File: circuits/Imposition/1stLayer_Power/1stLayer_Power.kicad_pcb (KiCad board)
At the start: 2 copper layers, 62.9 x 90.7 mm, 53 parts, among them J1 Conn_01x14_Pin, J11 Conn_01x02_Male, J12 Conn_01x02_Male, J2 Conn_01x14_Pin, J3 Conn_01x10_Socket, J4 Conn_01x02_Male, J5 Conn_01x02_Male, J6 Conn_01x02_Male, J7 Conn_01x14_Pin, J8 Conn_01x08_MountingPin, J9 Conn_01x08_MountingPin, Q1 2N7002, Q4 SQS141ELNW, Q6 SQS141ELNW, SW1 SW_SPDT

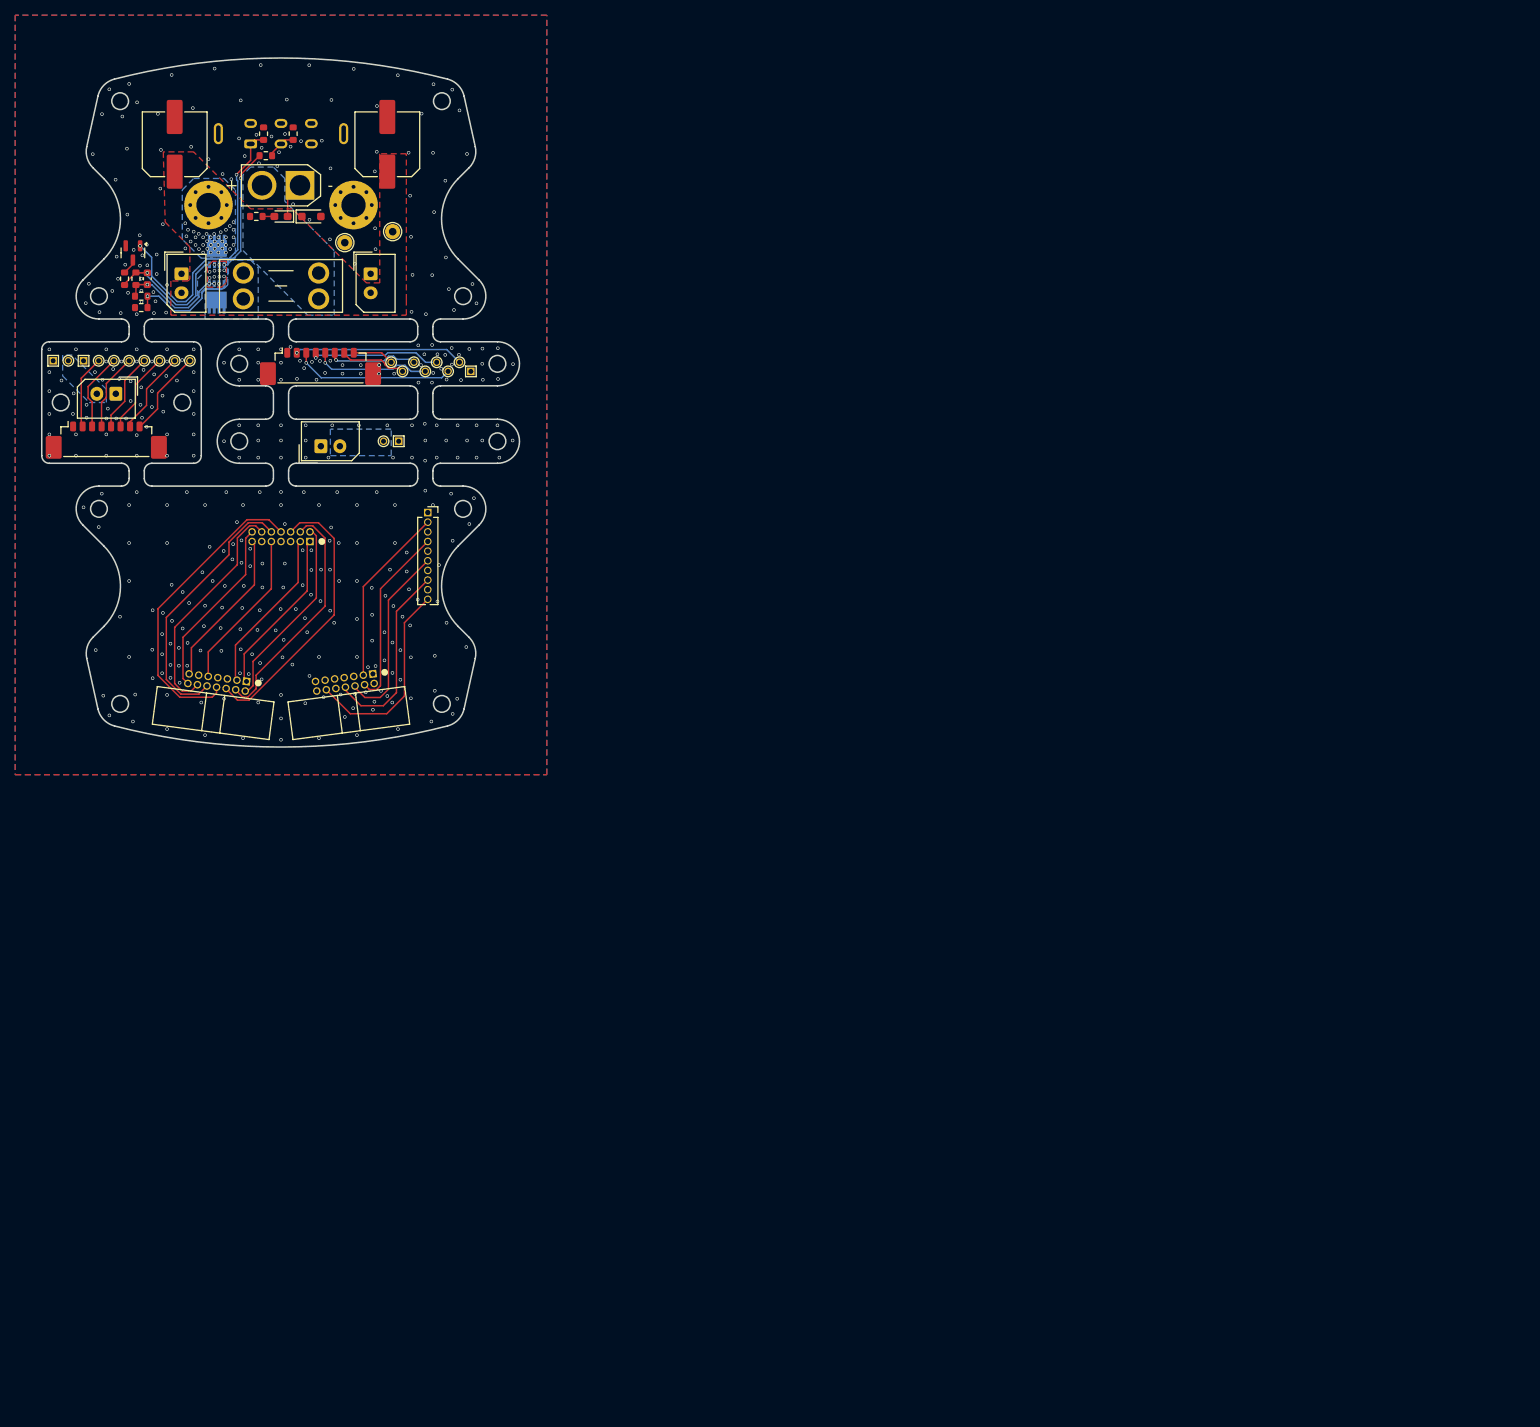
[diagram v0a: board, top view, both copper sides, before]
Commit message: 発注_第一弾
Drive, 1stLayer_Power, 2ndLayer_3rdLayer
を発注
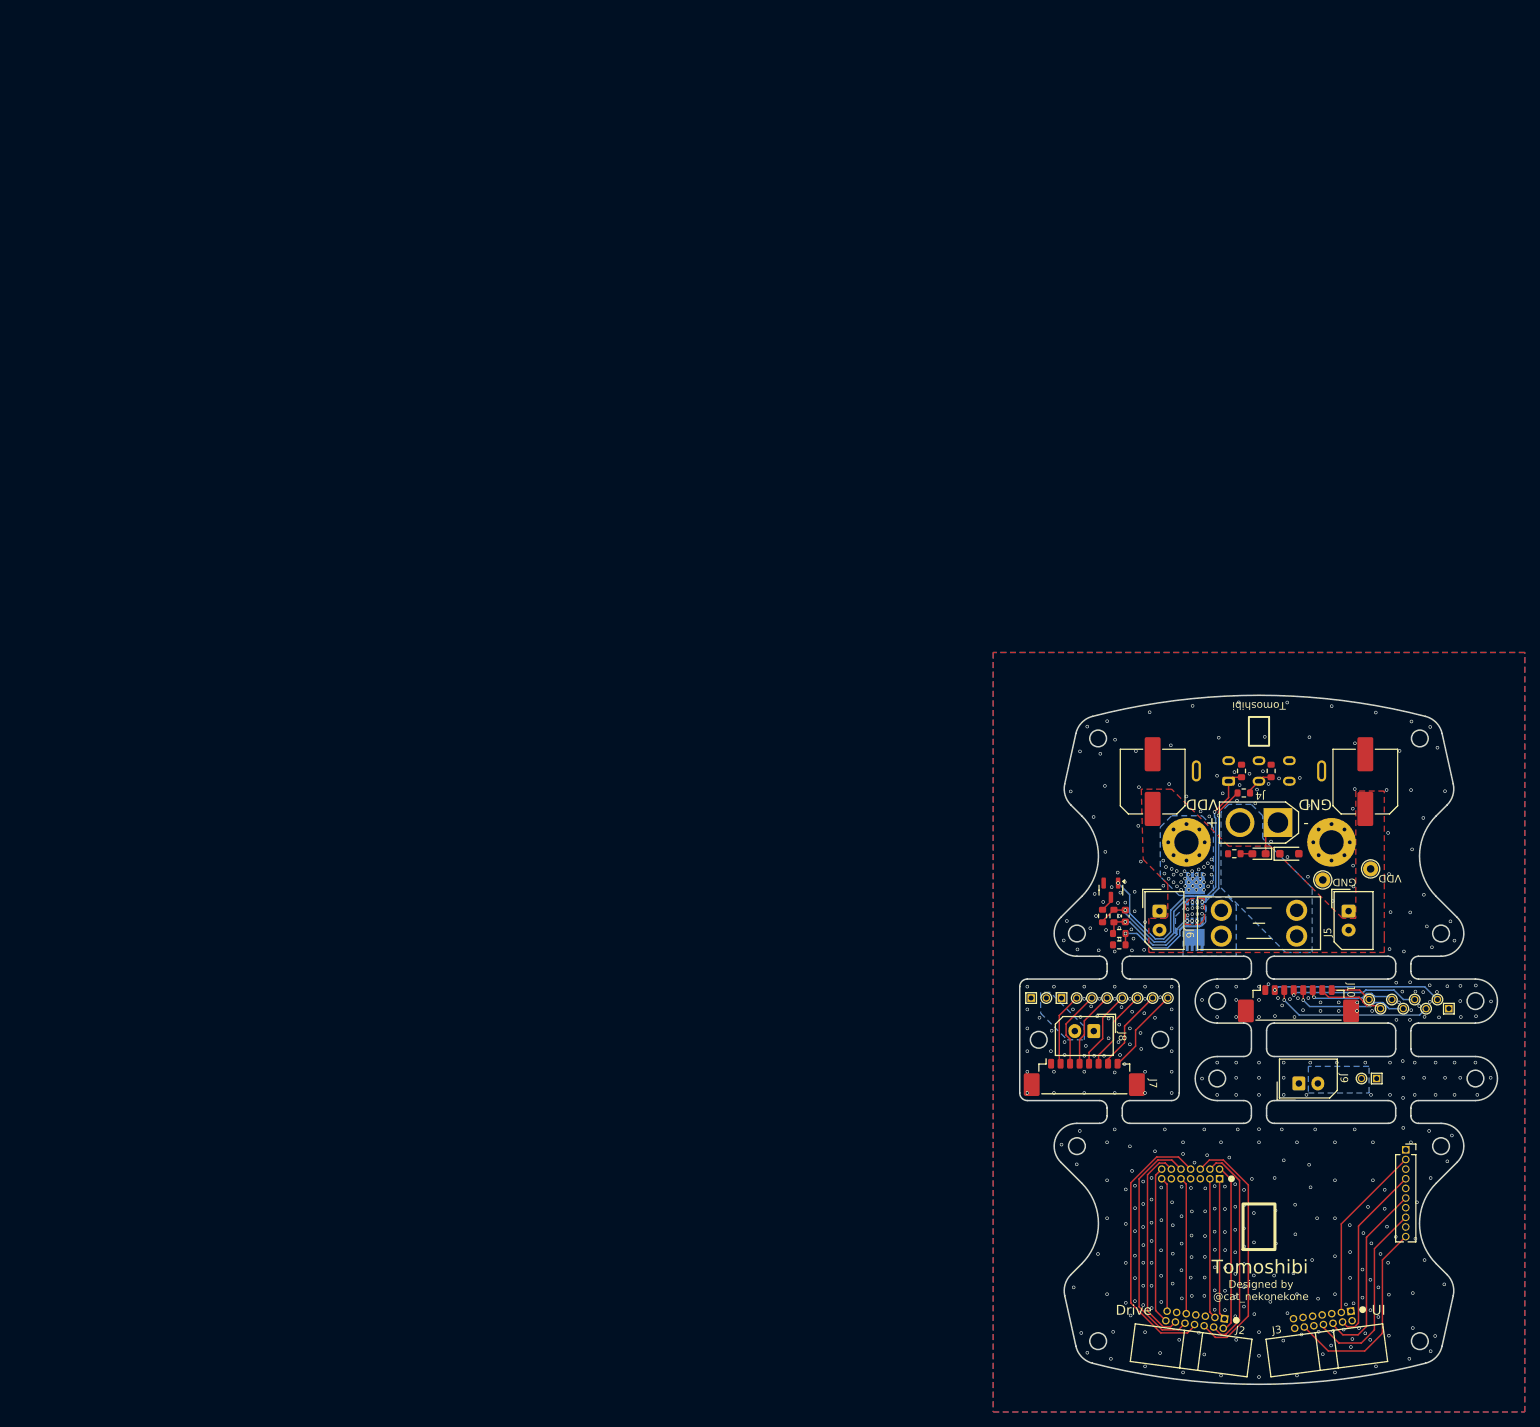
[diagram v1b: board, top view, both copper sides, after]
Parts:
- moved C1 153.7 mm to (142.8, 60.9)
- moved C3 153.7 mm to (111.2, 78.6)
- moved D2 153.7 mm to (132.8, 70.4)
- moved D3 153.7 mm to (128.8, 70.4)
- moved H11 153.7 mm to (153.8, 90.8)
- moved H12 153.7 mm to (152.3, 89.6)
- moved H13 153.7 mm to (150.8, 90.8)
- moved H14 153.7 mm to (149.3, 89.6)
- moved H15 153.7 mm to (147.8, 90.8)
- moved H16 153.7 mm to (146.3, 89.6)
- moved H17 153.7 mm to (144.8, 90.8)
- moved H18 153.7 mm to (143.3, 89.6)
- moved H21 153.7 mm to (144.3, 100.0)
- moved H22 153.7 mm to (142.3, 100.0)
- moved J10 153.7 mm to (134.0, 89.6)
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- renumbered J9 to J10, J3 to J11, J7 to J3, J8 to J7, J11 to J8, J12 to J9
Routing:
- net SWO_Drive: track 40.4 -> 36.3 mm
- net NRST_Drive: track 30.5 -> 26.8 mm
- net unconnected-(J1-Pin_10-Pad10): track 35.2 -> 31.6 mm
- net SWCLK_Drive: track 36.7 -> 33.1 mm
- net unconnected-(J1-Pin_1-Pad1): track 22.1 -> 18.7 mm
- net unconnected-(J1-Pin_13-Pad13): track 21.1 -> 17.7 mm
- net /1stLayer/3.3V_Drive: track 21.9 -> 18.5 mm
- net unconnected-(J1-Pin_2-Pad2): track 25.6 -> 22.3 mm
- net SWDIO_Drive: track 31.4 -> 28.2 mm
- net unconnected-(J1-Pin_9-Pad9): track 21.2 -> 18.0 mm
- net unconnected-(J1-Pin_14-Pad14): track 24.0 -> 20.8 mm
- net GND: vias 409 -> 437
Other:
- board text added: "Conn A"
- board text added: "Conn B"
- board text added: "Conn C"
- board text added: "Designed by @cat_nekonekone"
- board text added: "Drive"
- board text added: "GND"
- board text added: "JLCJLCJLCJLC"
- board text added: "Tomoshibi"
- board text added: "UI"
- board text added: "VDD"
- board text added: "燈"
